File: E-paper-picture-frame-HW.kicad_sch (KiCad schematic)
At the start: 0 parts

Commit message: Initial structure
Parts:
- added IC1: ESP32-C6-MINI-1-N4, ESP32C6MINI1N4, symbol ESP32-C6-MINI-1-N4:ESP32-C6-MINI-1-N4
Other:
- added sheet Display (display.kicad_sch)
- added sheet IO (IO.kicad_sch)

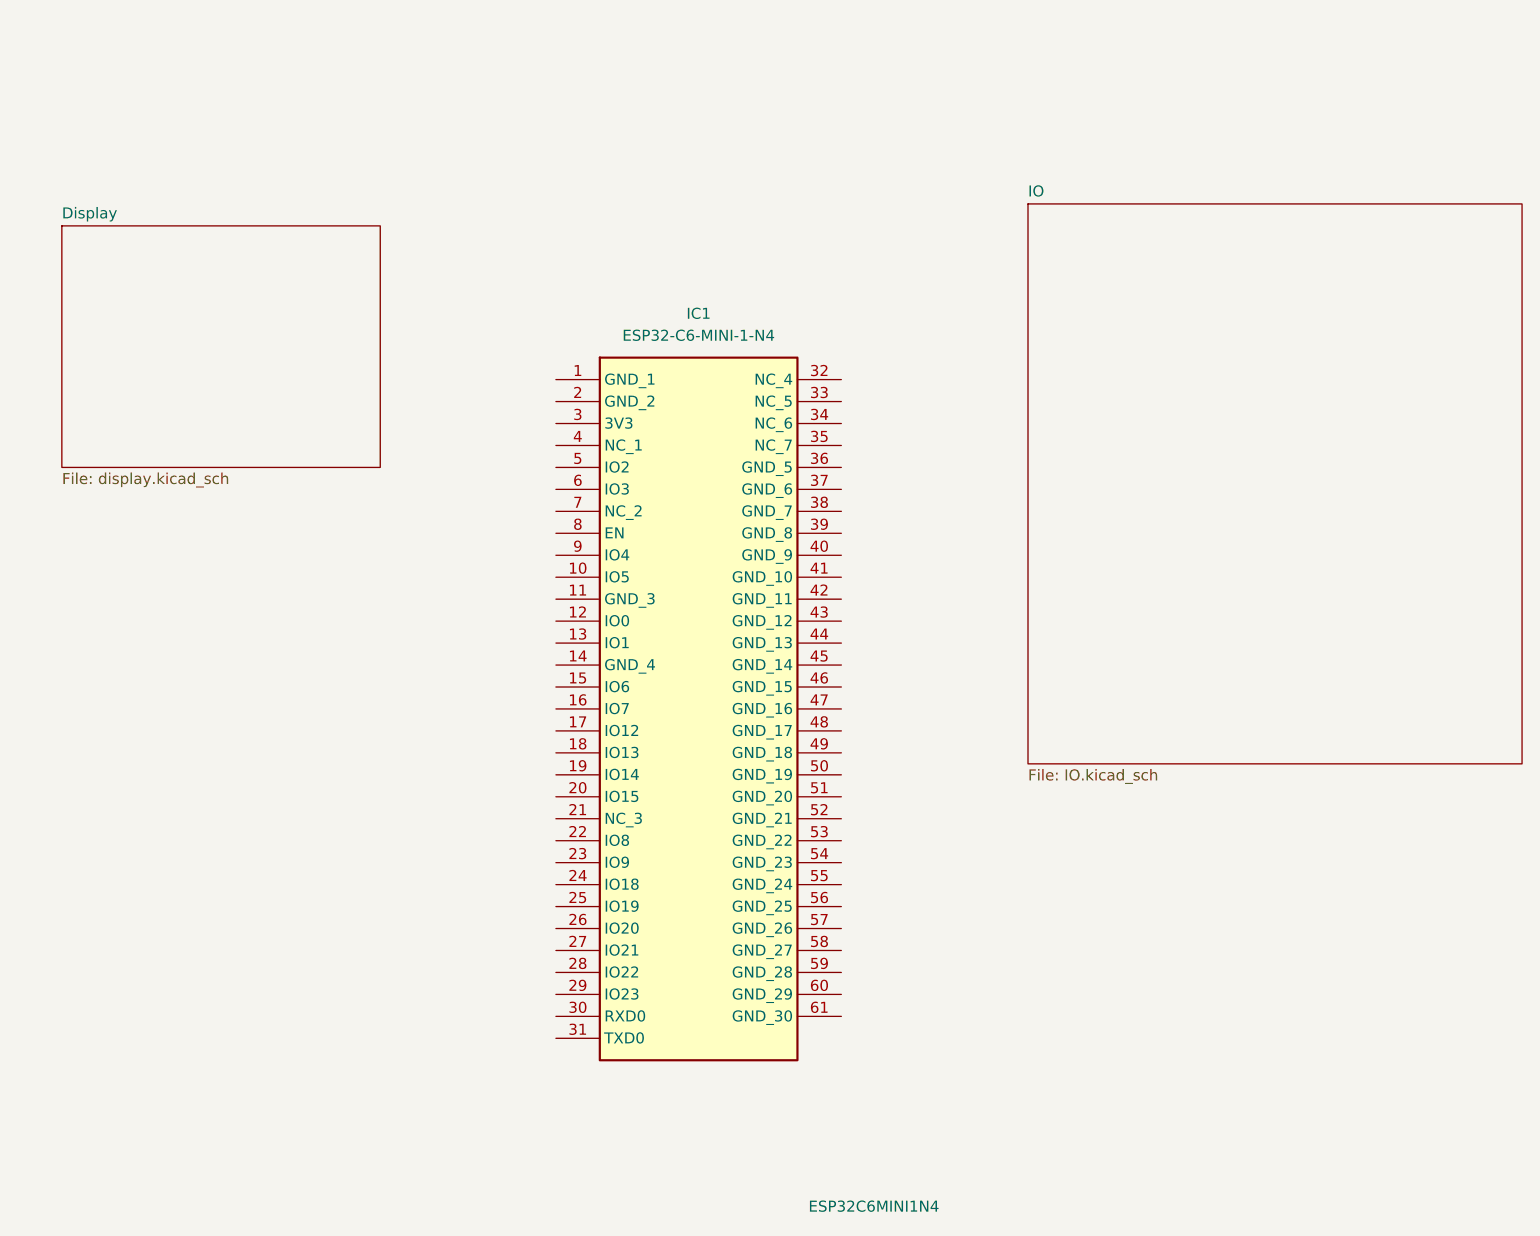
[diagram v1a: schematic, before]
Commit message: First draft of USB and power module Plus some display started
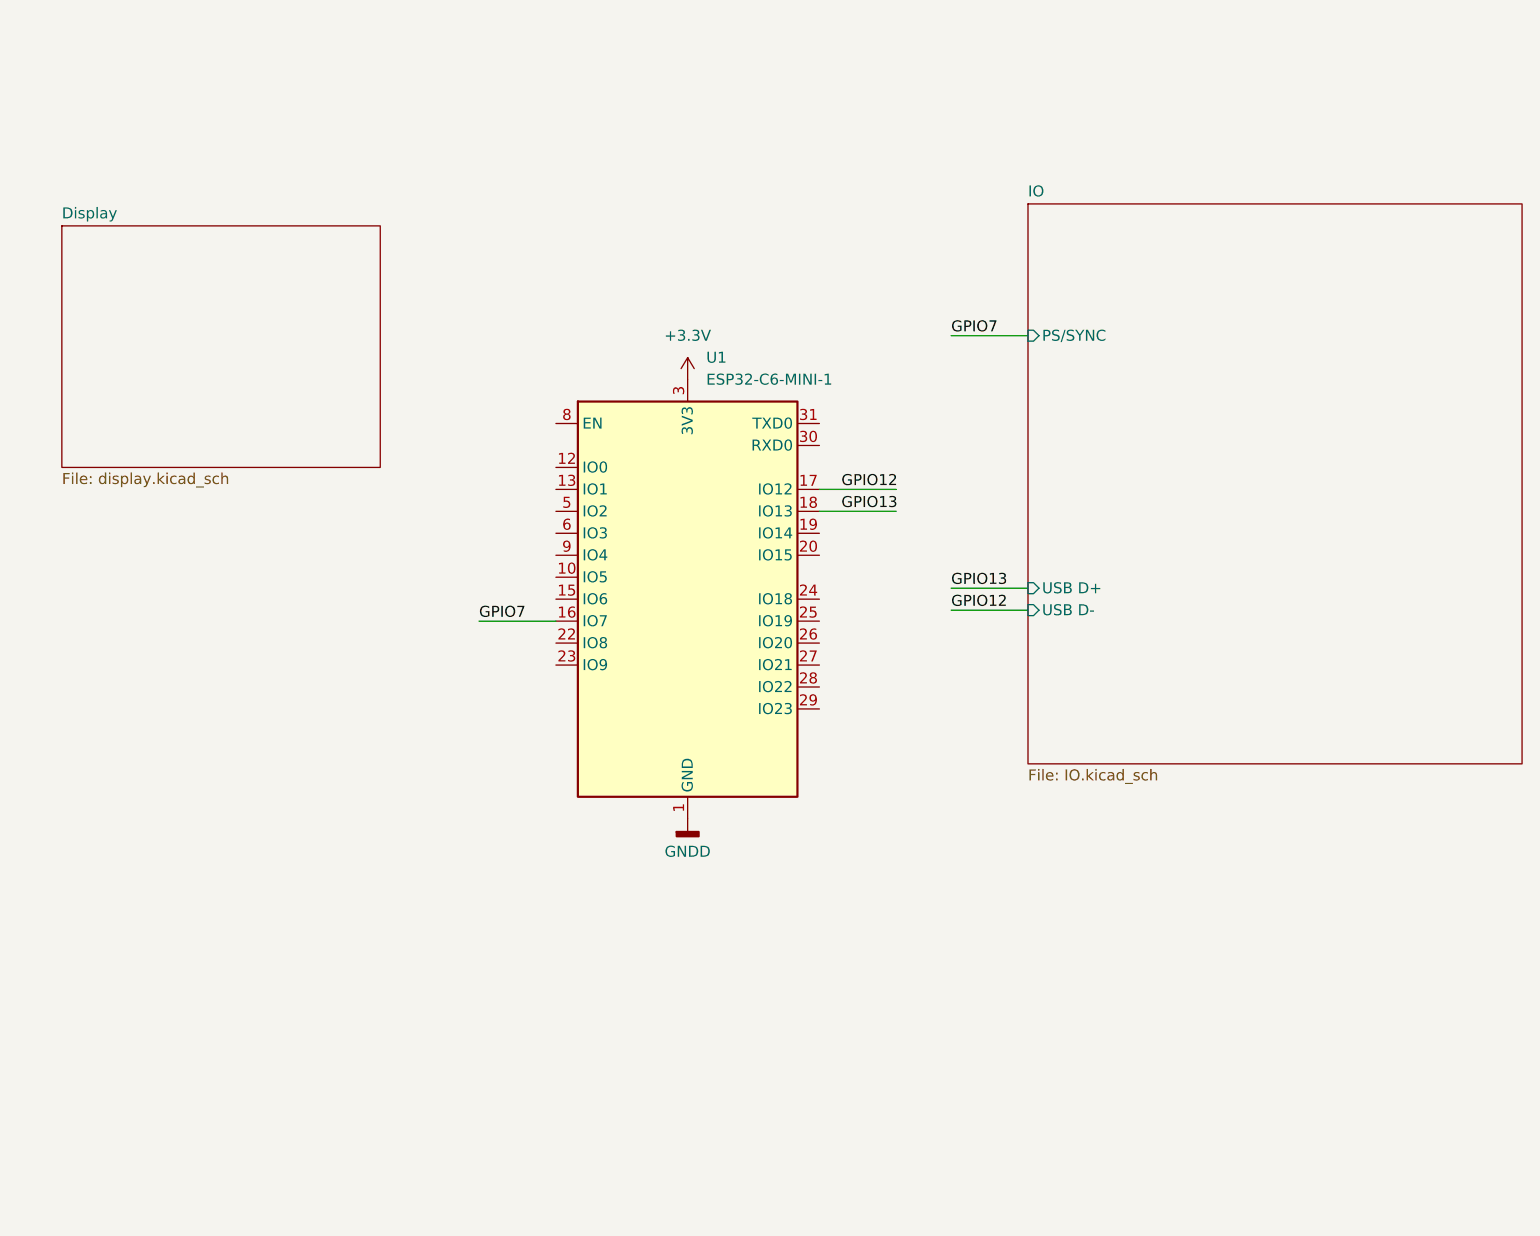
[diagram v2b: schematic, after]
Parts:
- removed IC1: ESP32-C6-MINI-1-N4, ESP32C6MINI1N4, symbol ESP32-C6-MINI-1-N4:ESP32-C6-MINI-1-N4
- added U1: ESP32-C6-MINI-1, RF_Module:ESP32-C6-MINI-1, symbol RF_Module:ESP32-C6-MINI-1
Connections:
- new net +3.3V: U1.3 (3V3)
- new net GNDD: U1.1 (GND), U1.11 (GND), U1.14 (GND), U1.2 (GND), U1.36 (GND), U1.37 (GND), U1.38 (GND), U1.39 (GND), U1.40 (GND), U1.41 (GND), U1.42 (GND), U1.43 (GND), U1.44 (GND), U1.45 (GND), U1.46 (GND), U1.47 (GND), U1.48 (GND), U1.49 (GND), U1.50 (GND), U1.51 (GND), U1.52 (GND), U1.53 (GND)
- new net GPIO12: U1.17 (IO12)
- new net GPIO13: U1.18 (IO13)
- new net GPIO7: U1.16 (IO7)
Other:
- sheet IO ports: added PS/SYNC, USB D+, USB D-; removed none

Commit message: Only missing Eframe - Mostly finished MCU - Added Test points to IO - Added LiPo charger - Added Power Source Selection - Added SD card module + SPI connections
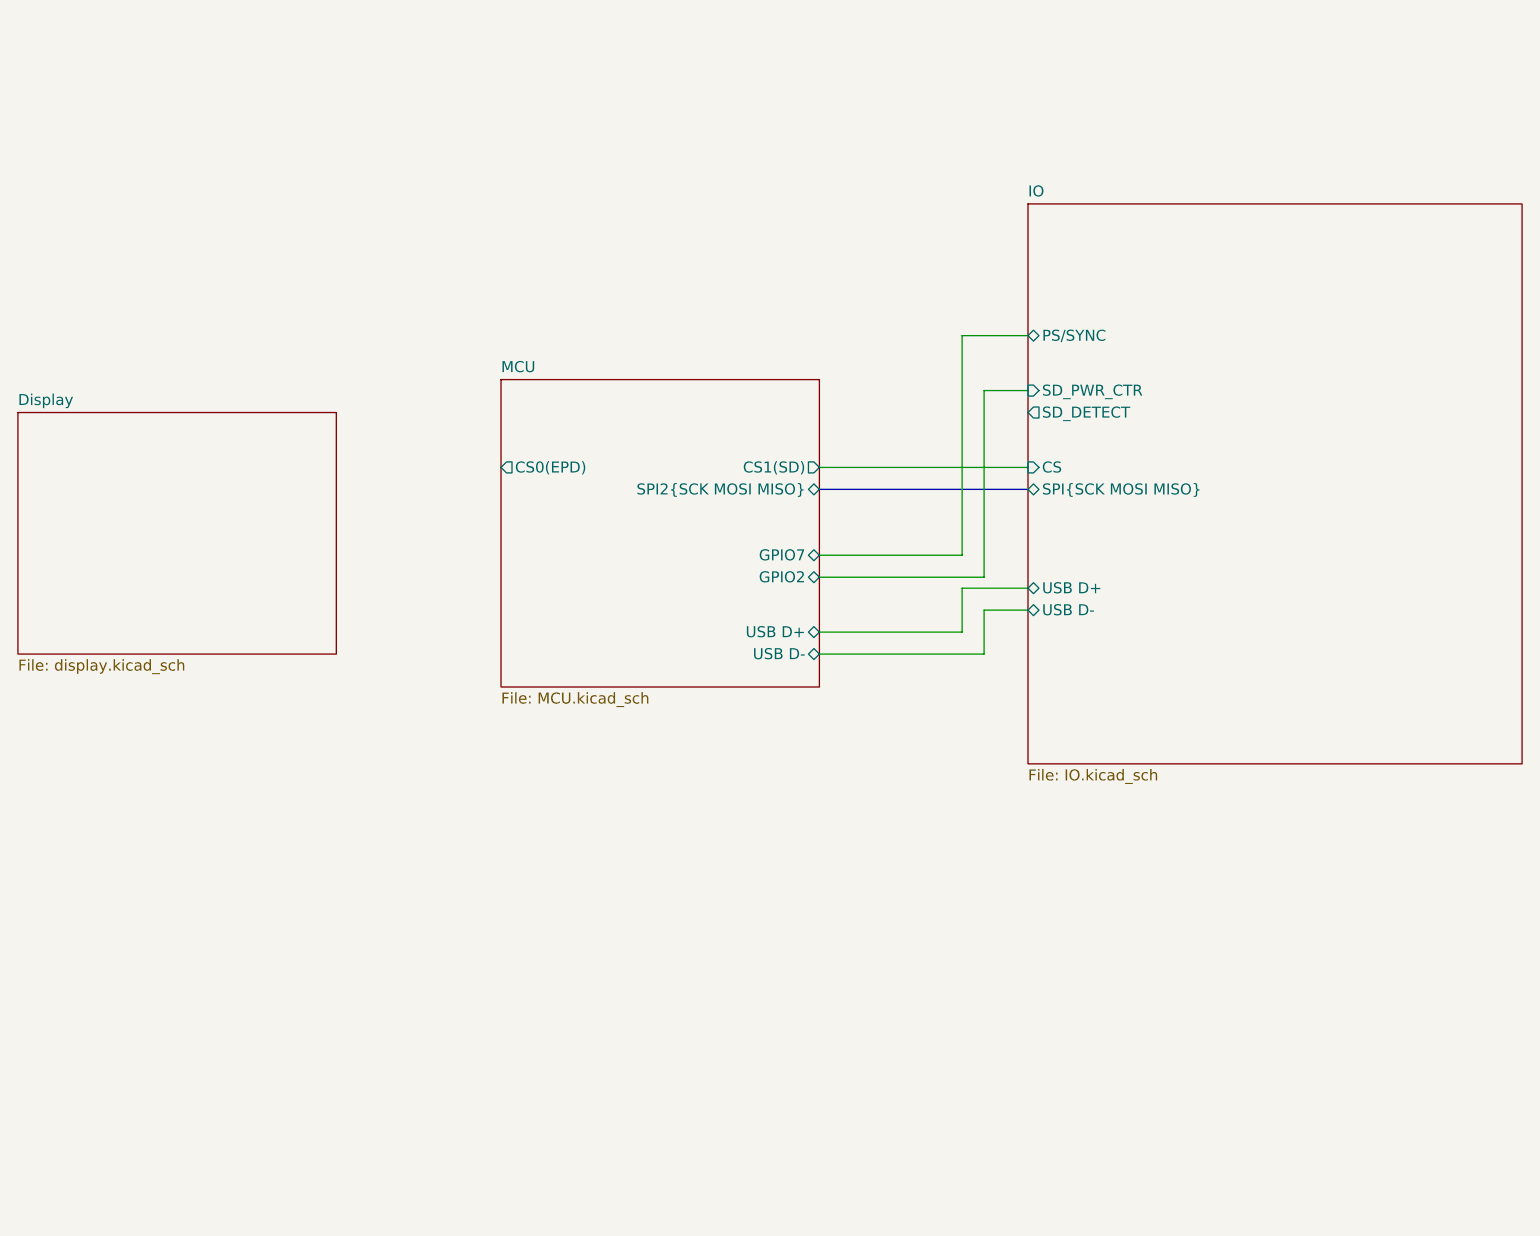
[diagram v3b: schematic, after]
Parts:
- removed U1: ESP32-C6-MINI-1, RF_Module:ESP32-C6-MINI-1, symbol RF_Module:ESP32-C6-MINI-1
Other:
- added sheet MCU (MCU.kicad_sch)
- sheet IO ports: added CS, SD_DETECT, SD_PWR_CTR, SPI{SCK MOSI MISO}; removed none

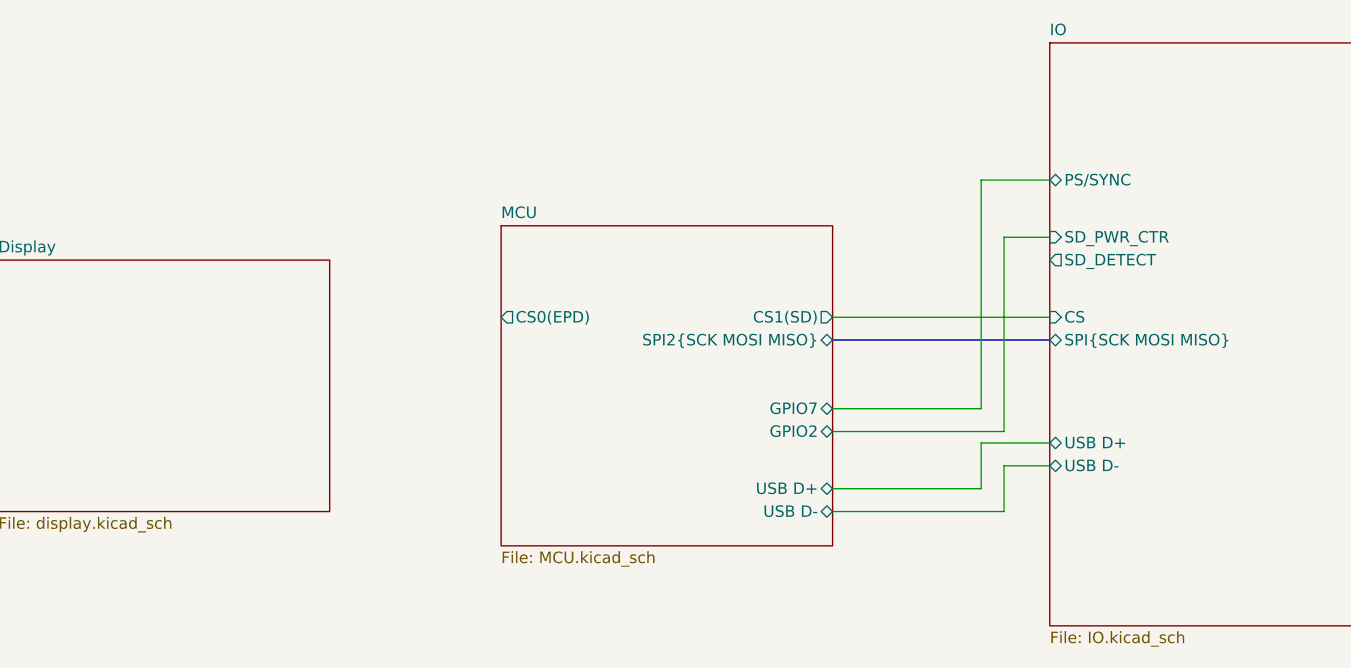
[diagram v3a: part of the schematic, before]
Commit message: Added eframe circuit: - Must replace 10uF caps with higher voltage rated ones - Should double check all the wiring - Assign MCU GPIOs now that all peripherals have their pins assigned
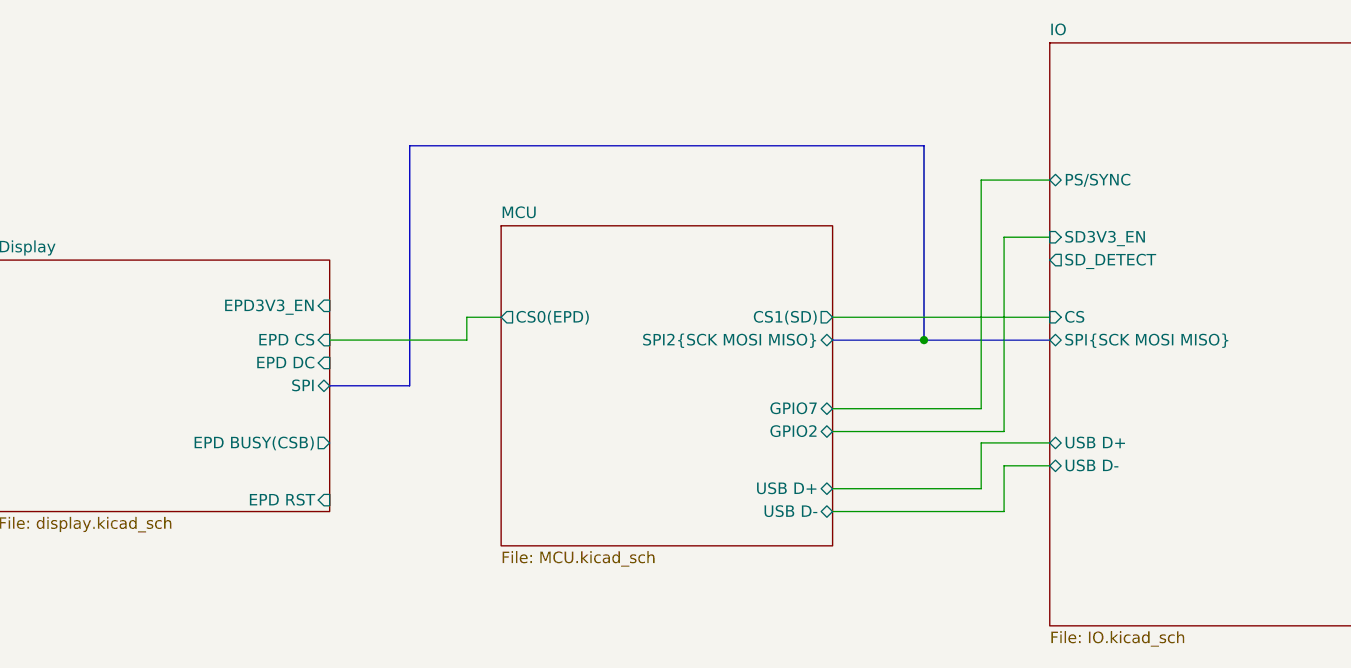
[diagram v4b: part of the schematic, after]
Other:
- sheet Display ports: added EPD BUSY(CSB), EPD CS, EPD DC, EPD RST, EPD3V3_EN, SPI; removed none
- sheet IO ports: added SD3V3_EN; removed SD_PWR_CTR
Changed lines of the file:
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@@
 	(generator_version "9.0")
 	(paper "A4")
+	(junction
+		(at 161.29 88.9)
+		(diameter 0)
+		(color 0 0 0 0)
+	)
+	(bus
+		(pts
+			(xy 104.14 93.98) (xy 104.14 67.31)
+		)
+		(stroke
+			(width 0)
+			(type default)
+		)
+	)
+	(bus
+		(pts
+			(xy 104.14 67.31) (xy 161.29 67.31)
+		)
+		(stroke
+			(width 0)
+			(type default)
+		)
+	)
 	(wire
 		(pts
@@
 	(wire
 		(pts
+			(xy 110.49 88.9) (xy 110.49 86.36)
+		)
+		(stroke
+			(width 0)
+			(type default)
+		)
+	)
+	(wire
+		(pts
 			(xy 151.13 99.06) (xy 170.18 99.06)
 		)
@@
 		)
 	)
+	(bus
+		(pts
+			(xy 161.29 67.31) (xy 161.29 88.9)
+		)
+		(stroke
+			(width 0)
+			(type default)
+		)
+	)
 	(wire
 		(pts
@@
 	(wire
 		(pts
+			(xy 110.49 86.36) (xy 114.3 86.36)
+		)
+		(stroke
+			(width 0)
+			(type default)
+		)
+	)
+	(wire
+		(pts
 			(xy 170.18 77.47) (xy 175.26 77.47)
 		)
@@
 		)
 	)
+	(bus
+		(pts
+			(xy 161.29 88.9) (xy 175.26 88.9)
+		)
+		(stroke
+			(width 0)
+			(type default)
+		)
+	)
+	(bus
+		(pts
+			(xy 95.25 93.98) (xy 104.14 93.98)
+		)
+		(stroke
+			(width 0)
+			(type default)
+		)
+	)
 	(wire
 		(pts
@@
 	(bus
 		(pts
-			(xy 151.13 88.9) (xy 175.26 88.9)
+			(xy 151.13 88.9) (xy 161.29 88.9)
 		)
 		(stroke
@@
 		(pts
 			(xy 167.64 96.52) (xy 167.64 71.12)
+		)
+		(stroke
+			(width 0)
+			(type default)
+		)
+	)
+	(wire
+		(pts
+			(xy 95.25 88.9) (xy 110.49 88.9)
 		)
 		(stroke
@@
 			)
 		)
+		(pin "EPD3V3_EN" input
+			(at 95.25 85.09 0)
+			(effects
+				(font
+					(size 1.27 1.27)
+				)
+				(justify right)
+			)
+		)
+		(pin "EPD BUSY(CSB)" output
+			(at 95.25 100.33 0)
+			(effects
+				(font
+					(size 1.27 1.27)
+				)
+				(justify right)
+			)
+		)
+		(pin "EPD RST" input
+			(at 95.25 106.68 0)
+			(effects
+				(font
+					(size 1.27 1.27)
+				)
+				(justify right)
+			)
+		)
+		(pin "EPD CS" input
+			(at 95.25 88.9 0)
+			(effects
+				(font
+					(size 1.27 1.27)
+				)
+				(justify right)
+			)
+		)
+		(pin "EPD DC" input
+			(at 95.25 91.44 0)
+			(effects
+				(font
+					(size 1.27 1.27)
+				)
+				(justify right)
+			)
+		)
+		(pin "SPI" bidirectional
+			(at 95.25 93.98 0)
+			(effects
+				(font
+					(size 1.27 1.27)
+				)
+				(justify right)
+			)
+		)
 		(instances
 			(project "E-paper-picture-frame-HW"
@@
 			)
 		)
-		(pin "SD_PWR_CTR" input
+		(pin "SD3V3_EN" input
 			(at 175.26 77.47 180)
 			(effects
